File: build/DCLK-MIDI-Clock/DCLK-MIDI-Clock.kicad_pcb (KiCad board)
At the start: 2 copper layers, 125 x 205 mm, 48 parts, among them J1 MIDI OUT, J2 Jack-DC, J3 MIDI OUT, J5 Conn_02x04_Odd_Even, J6 Conn_02x04_Odd_Even, SW4 RotaryEncoder_Switch_MP, U2 CAP1206-x-SL

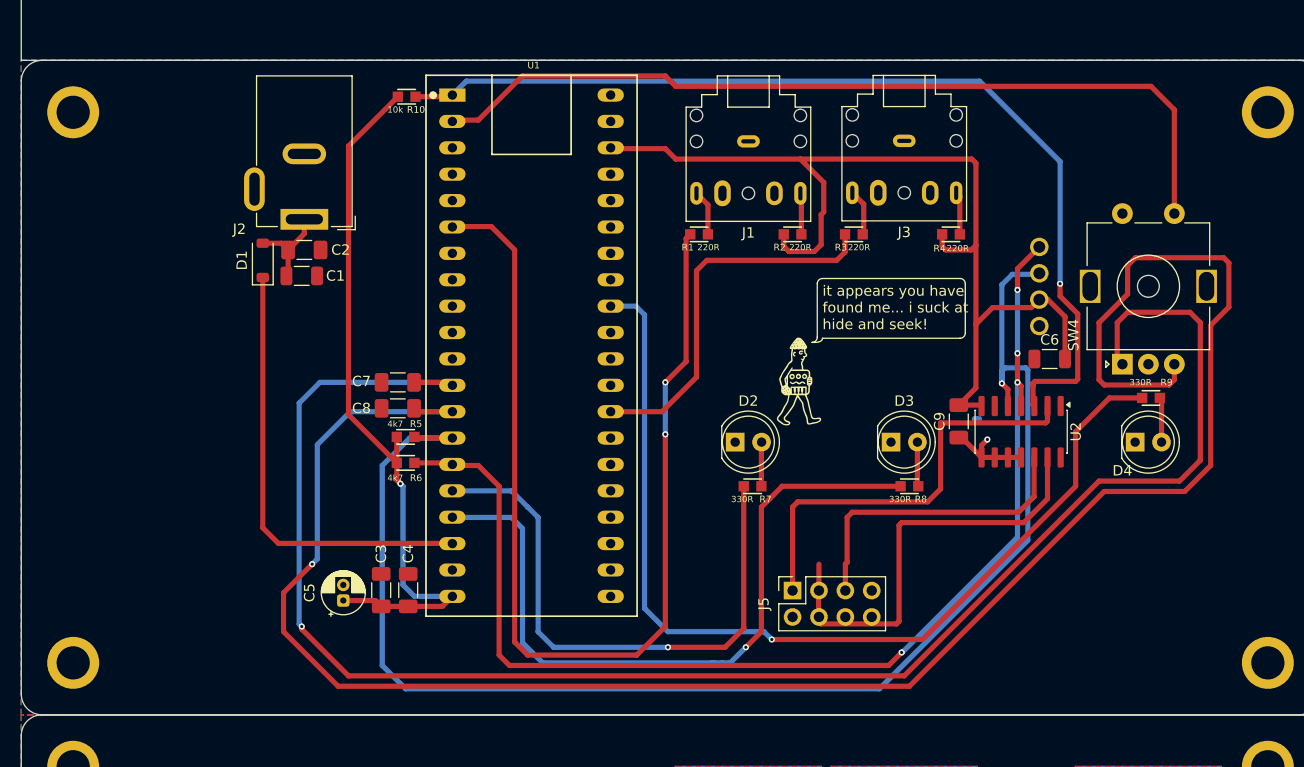
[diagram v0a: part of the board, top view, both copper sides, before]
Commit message: PCB update
-Added 2x Sync Output
-Moved 5V DC in
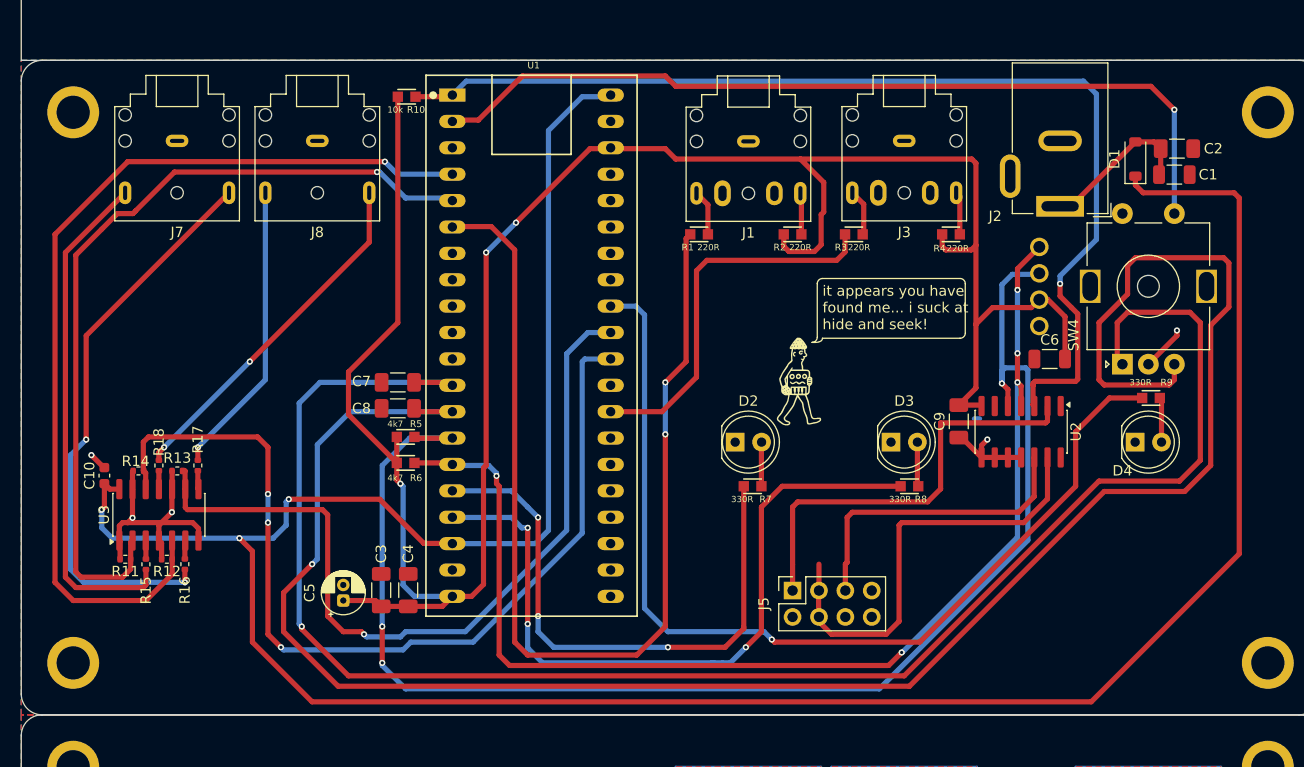
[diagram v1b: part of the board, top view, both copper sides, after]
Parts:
- added C10: 100nF, Capacitor_SMD:C_0603_1608Metric, F.Cu at (26.0, 64.0)
- added J7: SYNC 1 OUT, PJ307-TRS:PJ307-TRS-SOCKET, F.Cu at (33.0, 31.8)
- added J8: SYNC 2 OUT, PJ307-TRS:PJ307-TRS-SOCKET, F.Cu at (46.5, 31.8)
- added R11: 100k, Resistor_SMD:R_0402_1005Metric, F.Cu at (28.0, 72.0)
- added R12: 100k, Resistor_SMD:R_0402_1005Metric, F.Cu at (32.0, 72.0)
- added R13: 100k, Resistor_SMD:R_0402_1005Metric, F.Cu at (33.0, 63.5)
- added R14: 100k, Resistor_SMD:R_0402_1005Metric, F.Cu at (29.3, 63.5)
- added R15: 1k, Resistor_SMD:R_0402_1005Metric, F.Cu at (30.0, 72.5)
- added R16: 1k, Resistor_SMD:R_0402_1005Metric, F.Cu at (33.8, 72.5)
- added R17: 1k, Resistor_SMD:R_0402_1005Metric, F.Cu at (35.0, 63.0)
- added R18: 1k, Resistor_SMD:R_0402_1005Metric, F.Cu at (31.2, 63.0)
- added U3: 74AHCT125, Package_SO:SOIC-14_3.9x8.7mm_P1.27mm, F.Cu at (31.2, 67.8)
- moved C1 84.6 mm to (129.0, 35.0)
- moved C2 84.6 mm to (129.2, 32.5)
- moved D1 84.6 mm to (125.2, 33.5)
- moved J2 72.8 mm to (118.0, 38.0)
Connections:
- U1 pad 30: unconnected-(U1-PA4/ADC4-Pad30) -> RUN2
- U1 pad 31: unconnected-(U1-PA5/ADC5/SCK1-Pad31) -> SYNC2
- U1 pad 4: unconnected-(U1-PB15/MOSI2-Pad4) -> RUN1
- U1 pad 5: unconnected-(U1-PA8-Pad5) -> SYNC1
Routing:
- net Vcc: track 43.0 -> 259.9 mm, vias 0 -> 3
- net RUN1: track 0.00 -> 91.5 mm, vias 0 -> 1
- net RUN2: track 0.00 -> 90.1 mm, vias 0 -> 3
- net SYNC1: track 0.00 -> 79.8 mm, vias 0 -> 1
- net SYNC2: track 0.00 -> 77.7 mm, vias 0 -> 1
- net /RUN1_OUT: track 0.00 -> 55.3 mm, vias 0 -> 2
- net 3V3: track 165.7 -> 217.4 mm, vias 1 -> 3
- net /SYNC1_OUT: track 0.00 -> 49.1 mm
- net /RUN2_OUT: track 0.00 -> 34.1 mm, vias 0 -> 2
- net GND: track 9.25 -> 42.1 mm, vias 1 -> 5
- net /SYNC2_OUT: track 0.00 -> 28.4 mm, vias 0 -> 1
- net ISR: track 94.2 -> 103.0 mm
- net Net-(D1-A): track 8.87 -> 14.9 mm
- net Net-(U3-3Y): track 0.00 -> 1.79 mm
- net Net-(U3-1Y): track 0.00 -> 1.78 mm
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
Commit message: sch and pcb tweaks
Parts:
- added REF**: Faceplate_Hole_LED_Button_5.4mm_With_Mask_Opening, PCM_4ms_Faceplate:Faceplate_Hole_LED_Button_5.4mm_With_Mask_Opening, F.Cu at (103.0, 113.2)
- added REF**: Faceplate_Hole_LED_Button_5.4mm_With_Mask_Opening, PCM_4ms_Faceplate:Faceplate_Hole_LED_Button_5.4mm_With_Mask_Opening, F.Cu at (88.0, 113.2)
- added REF**: Faceplate_Hole_LED_Button_5.4mm_With_Mask_Opening, PCM_4ms_Faceplate:Faceplate_Hole_LED_Button_5.4mm_With_Mask_Opening, F.Cu at (126.5, 113.2)
- R1, R2, R3, R4: value 220R -> 33R
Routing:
- net CH2: track 53.5 -> 51.0 mm
- net SETTINGS: track 62.0 -> 64.5 mm
- net CH1: track 50.9 -> 53.4 mm
- net unconnected-(J5-Pin_8-Pad8): track 0.00 -> 1.96 mm

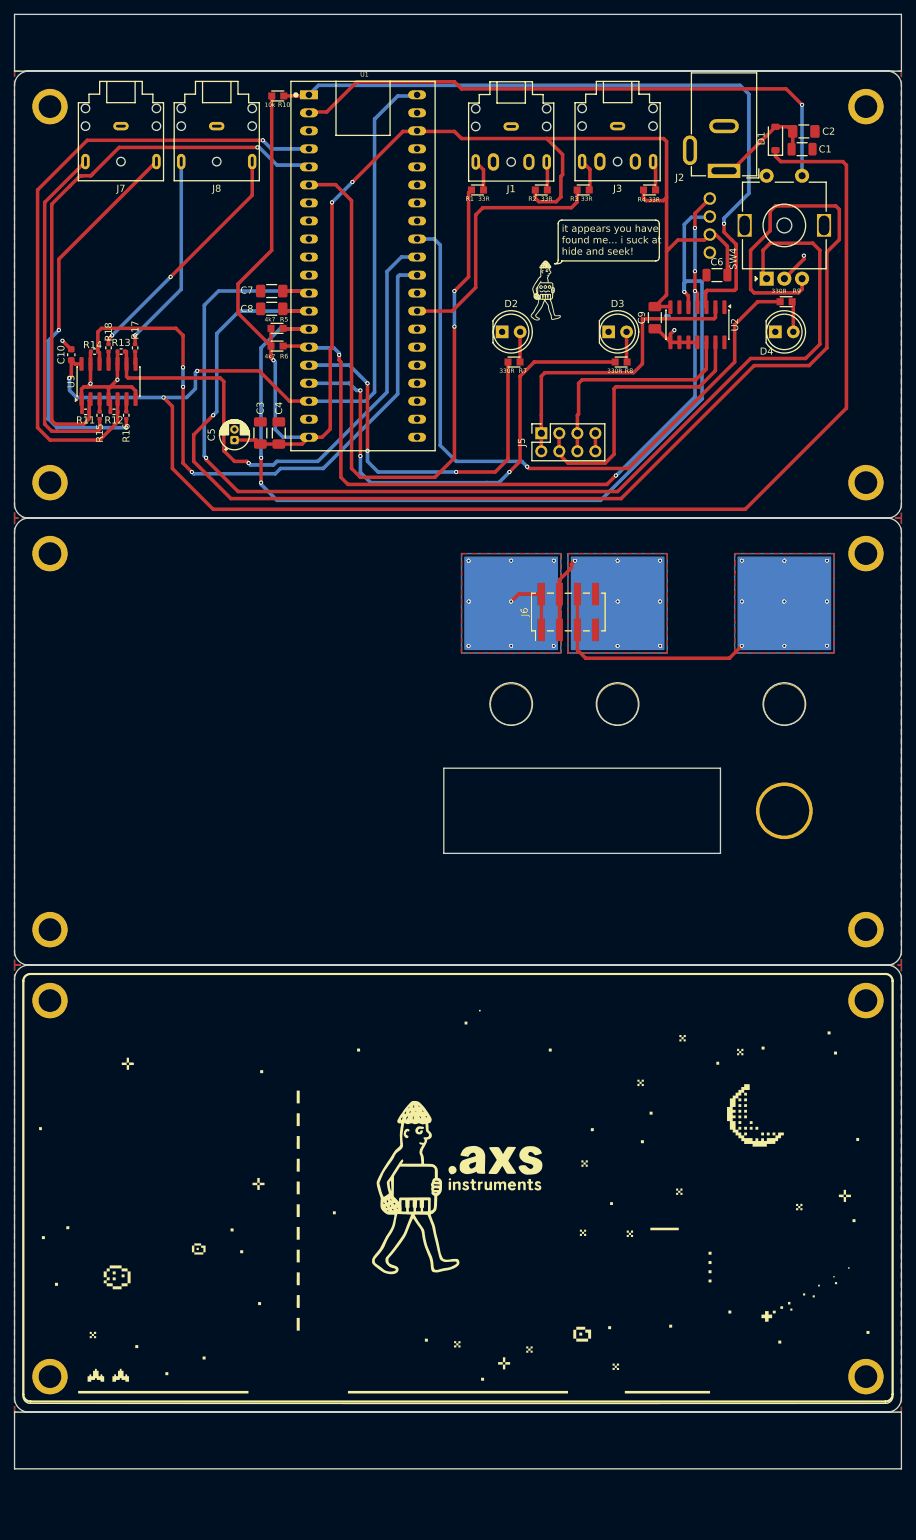
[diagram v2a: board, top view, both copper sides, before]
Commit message: added mouse bites
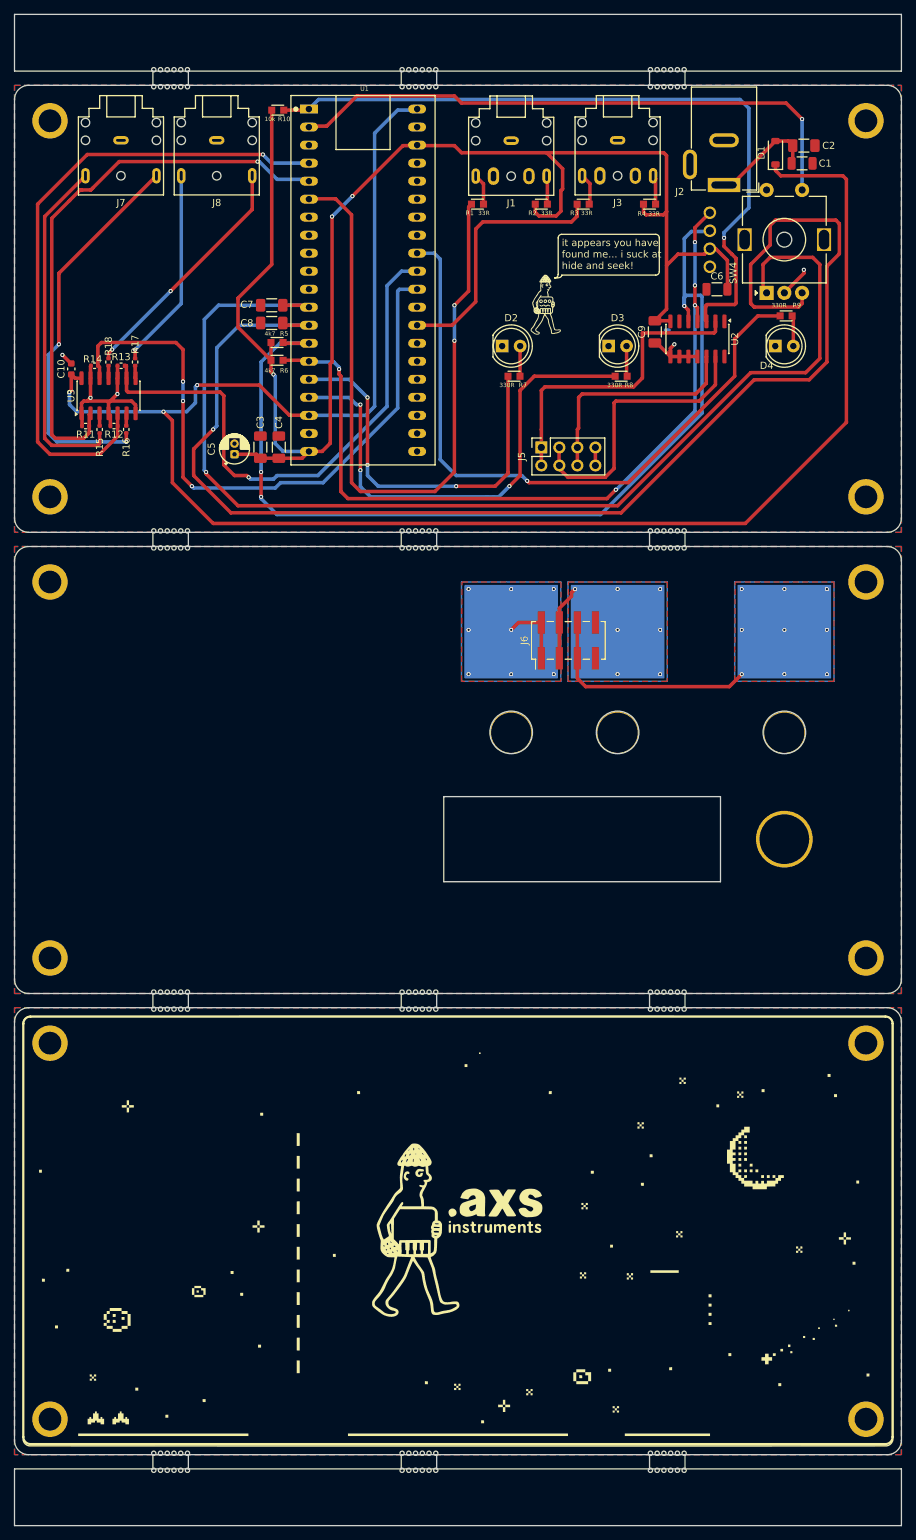
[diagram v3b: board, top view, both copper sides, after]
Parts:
- added MB**: MouseBite_Tab, mouse bites:MouseBite_Tab_5mm_Gap2mm, F.Cu at (75.0, 220.0)
- added MB**: MouseBite_Tab, mouse bites:MouseBite_Tab_5mm_Gap2mm, F.Cu at (110.0, 220.0)
- added MB**: MouseBite_Tab, mouse bites:MouseBite_Tab_5mm_Gap2mm, F.Cu at (40.0, 220.0)
- added MB**: MouseBite_Tab, mouse bites:MouseBite_Tab_5mm_Gap2mm, F.Cu at (40.0, 155.0)
- added MB**: MouseBite_Tab, mouse bites:MouseBite_Tab_5mm_Gap2mm, F.Cu at (40.0, 90.0)
- added MB**: MouseBite_Tab, mouse bites:MouseBite_Tab_5mm_Gap2mm, F.Cu at (75.0, 25.0)
- added MB**: MouseBite_Tab, mouse bites:MouseBite_Tab_5mm_Gap2mm, F.Cu at (75.0, 90.0)
- added MB**: MouseBite_Tab, mouse bites:MouseBite_Tab_5mm_Gap2mm, F.Cu at (110.0, 90.0)
- added MB**: MouseBite_Tab, mouse bites:MouseBite_Tab_5mm_Gap2mm, F.Cu at (75.0, 155.0)
- added MB**: MouseBite_Tab, mouse bites:MouseBite_Tab_5mm_Gap2mm, F.Cu at (110.0, 155.0)
- added MB**: MouseBite_Tab, mouse bites:MouseBite_Tab_5mm_Gap2mm, F.Cu at (110.0, 25.0)
- added MB**: MouseBite_Tab, mouse bites:MouseBite_Tab_5mm_Gap2mm, F.Cu at (40.0, 25.0)
- moved ? 6.00 mm to (138.0, 214.0)
- moved ? 6.00 mm to (138.0, 161.0)
- moved ? 6.00 mm to (23.0, 214.0)
- moved ? 6.00 mm to (23.0, 161.0)
- moved G*** 6.00 mm to (80.5, 187.5)
- moved ? 4.00 mm to (138.0, 96.0)
- moved ? 4.00 mm to (23.0, 96.0)
- moved ? 4.00 mm to (138.0, 149.0)
- moved ? 4.00 mm to (23.0, 149.0)
- moved G*** 4.00 mm to (80.5, 122.5)
- moved J6 4.00 mm to (96.1, 104.2)
- moved REF** 4.00 mm to (103.0, 117.2)
- moved REF** 4.00 mm to (88.0, 117.2)
- moved REF** 4.00 mm to (126.5, 117.2)
- moved REF** 4.00 mm to (126.5, 132.2)
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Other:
- board size 125 x 205 mm -> 125 x 213 mm

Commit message: mouse bites
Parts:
- removed the MB** at (75.0, 220.0)
- removed the MB** at (110.0, 220.0)
- removed the MB** at (40.0, 220.0)
- removed the MB** at (40.0, 155.0)
- removed the MB** at (40.0, 90.0)
- removed the MB** at (75.0, 25.0)
- removed the MB** at (75.0, 90.0)
- removed the MB** at (110.0, 90.0)
- removed the MB** at (75.0, 155.0)
- removed the MB** at (110.0, 155.0)
- removed the MB** at (110.0, 25.0)
- removed the MB** at (40.0, 25.0)
- added MB**: MouseBite_Tab, mouse bites:MouseBite_Tab_5mm_Gap2mm, F.Cu at (80.5, 25.0)
- added MB**: MouseBite_Tab, mouse bites:MouseBite_Tab_5mm_Gap2mm, F.Cu at (80.5, 90.0)
- added MB**: MouseBite_Tab, mouse bites:MouseBite_Tab_5mm_Gap2mm, F.Cu at (120.5, 220.0)
- added MB**: MouseBite_Tab, mouse bites:MouseBite_Tab_5mm_Gap2mm, F.Cu at (40.5, 155.0)
- added MB**: MouseBite_Tab, mouse bites:MouseBite_Tab_5mm_Gap2mm, F.Cu at (40.5, 25.0)
- added MB**: MouseBite_Tab, mouse bites:MouseBite_Tab_5mm_Gap2mm, F.Cu at (80.5, 155.0)
- added MB**: MouseBite_Tab, mouse bites:MouseBite_Tab_5mm_Gap2mm, F.Cu at (120.5, 90.0)
- added MB**: MouseBite_Tab, mouse bites:MouseBite_Tab_5mm_Gap2mm, F.Cu at (40.5, 220.0)
- added MB**: MouseBite_Tab, mouse bites:MouseBite_Tab_5mm_Gap2mm, F.Cu at (80.5, 220.0)
- added MB**: MouseBite_Tab, mouse bites:MouseBite_Tab_5mm_Gap2mm, F.Cu at (120.5, 25.0)
- added MB**: MouseBite_Tab, mouse bites:MouseBite_Tab_5mm_Gap2mm, F.Cu at (40.5, 90.0)
- added MB**: MouseBite_Tab, mouse bites:MouseBite_Tab_5mm_Gap2mm, F.Cu at (120.5, 155.0)
